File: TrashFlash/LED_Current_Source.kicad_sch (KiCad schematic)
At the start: 32 parts, among them IC2 ADG5419BCPZ-RL7, IC4 SN74LXC2T45QDTTRQ1, IC8 AD8615AUJZ-REEL, Q1 BC56-10PA,115, Q2 BC56-10PA,115, Q3 BC56-10PA,115, Q4 BC56-10PA,115, U1 SI5448DU-T1-GE3, U2 SI5448DU-T1-GE3

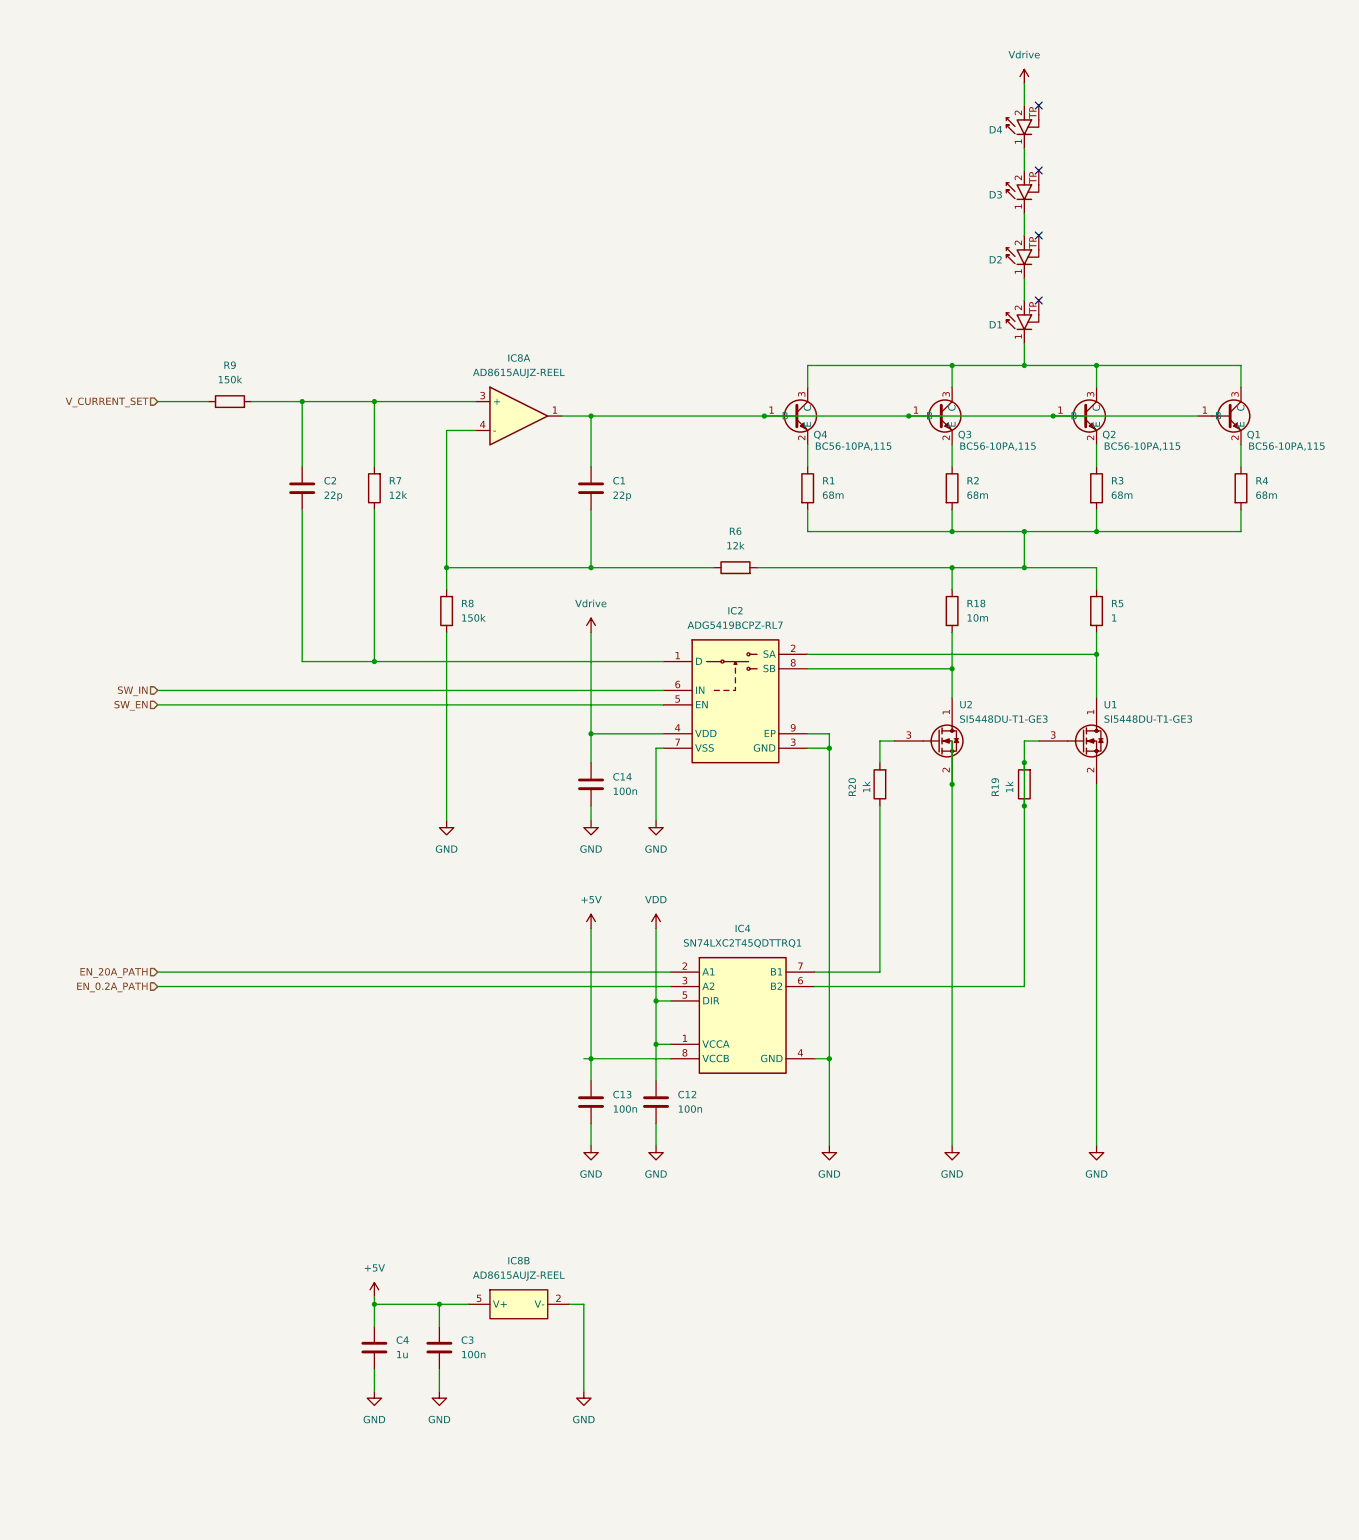
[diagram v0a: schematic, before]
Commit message: Added netlabels / cleaned up schematic
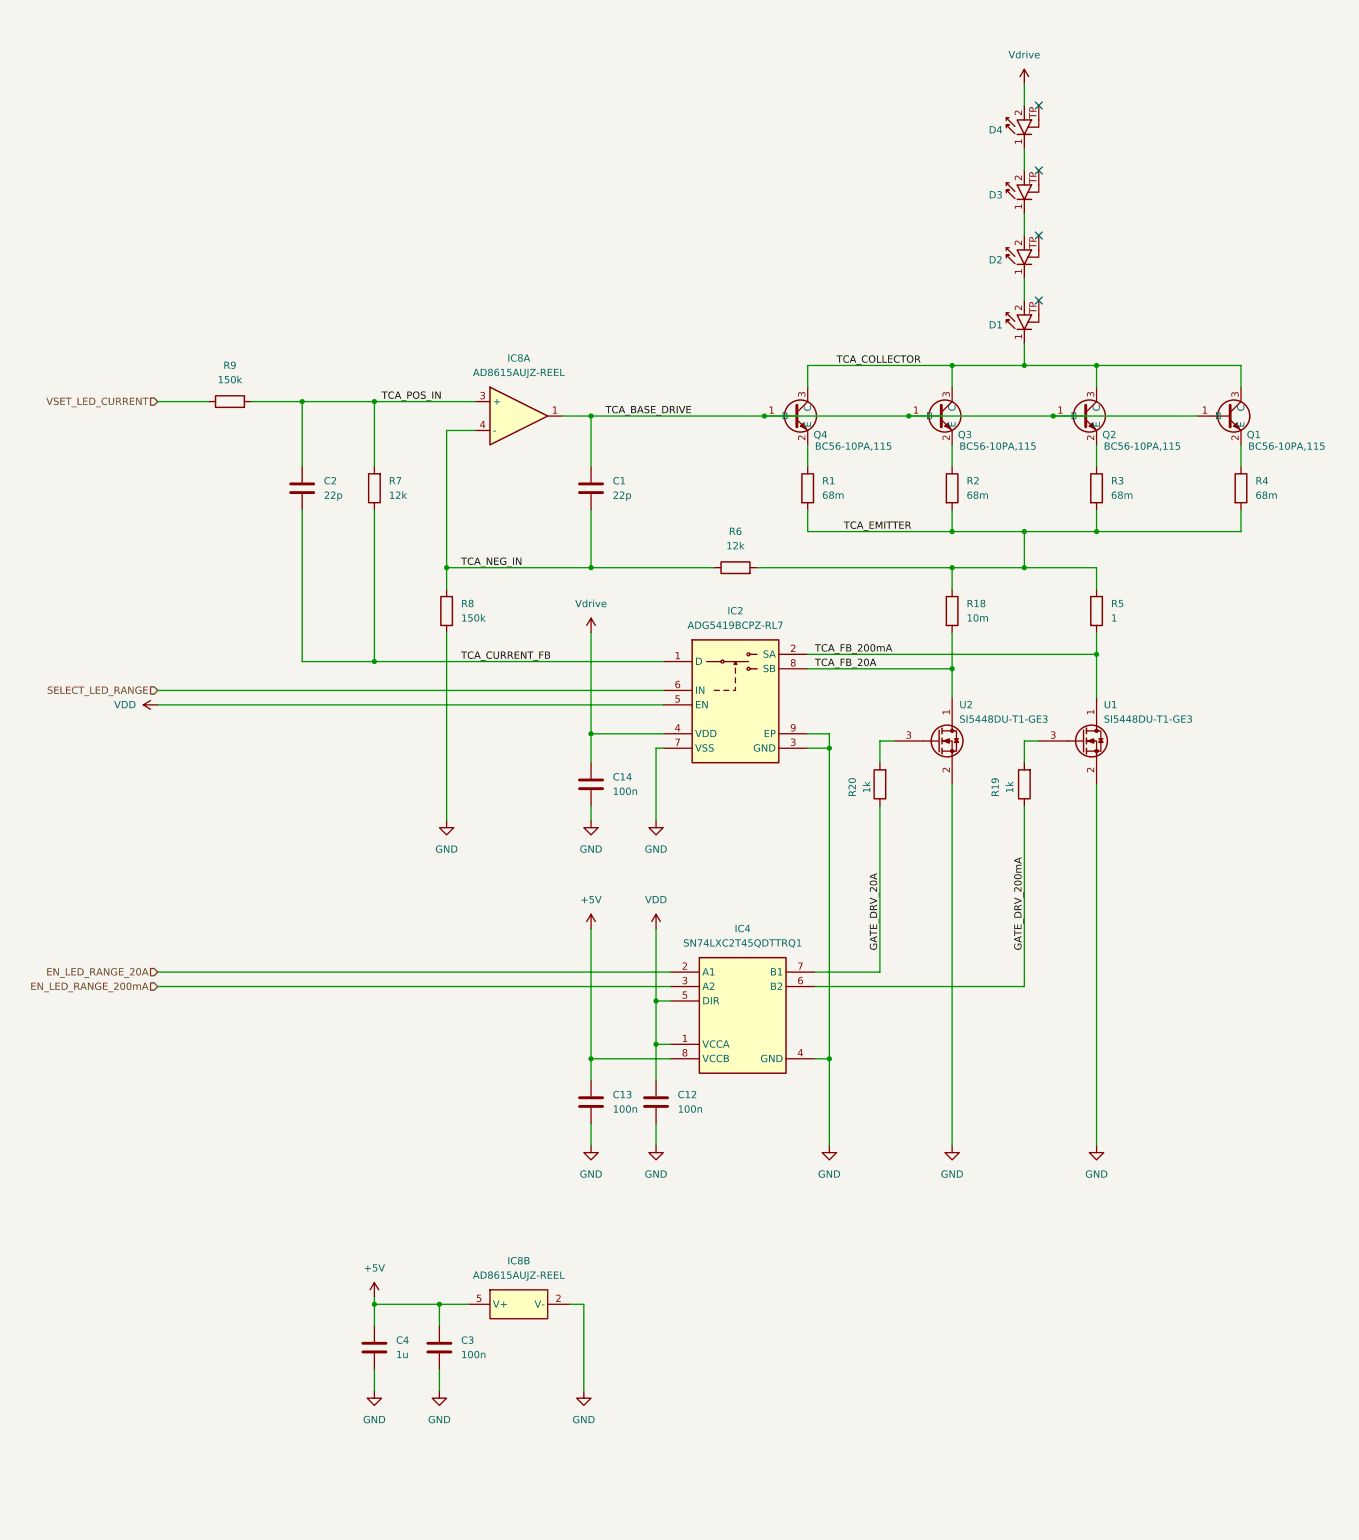
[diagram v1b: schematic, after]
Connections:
- net SW_EN is gone; now on net VDD: IC2.5 (EN)
- net TCA_FB_20A: now reaches IC2.8 (SB), R18.2, U2.1
- net TCA_EMITTER: now reaches R1.2, R18.1, R2.2, R3.2, R4.2, R5.1, R6.2
- net TCA_NEG_IN: now reaches C1.2, IC8.4 (-), R6.1, R8.2
- net TCA_CURRENT_FB: now reaches C2.1, IC2.1 (D), R7.1
- net TCA_FB_200mA: now reaches IC2.2 (SA), R5.2, U1.1
- net TCA_BASE_DRIVE: now reaches C1.1, IC8.1, Q1.1 (B), Q2.1 (B), Q3.1 (B), Q4.1 (B)
- net TCA_COLLECTOR: now reaches D1.1 (K), Q1.3 (C), Q2.3 (C), Q3.3 (C), Q4.3 (C)
- net at R19.2, U1.3: no longer IC4.6 (B2), R19.1
- net TCA_POS_IN: now reaches C2.2, IC8.3 (+), R7.2, R9.2
- net GATE_DRV_20A: now reaches IC4.7 (B1), R20.1
- net EN_0.2A_PATH renamed EN_LED_RANGE_200mA
- net EN_20A_PATH renamed EN_LED_RANGE_20A
- net SW_IN renamed SELECT_LED_RANGE
- net V_CURRENT_SET renamed VSET_LED_CURRENT
- new net GATE_DRV_200mA: IC4.6 (B2), R19.1
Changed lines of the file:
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@@
 	)
 	(junction
-		(at 276.86 144.78)
-		(diameter 0)
-		(color 0 0 0 0)
-	)
-	(junction
 		(at 276.86 110.49)
 		(diameter 0)
@@
 	)
 	(junction
-		(at 276.86 152.4)
-		(diameter 0)
-		(color 0 0 0 0)
-	)
-	(junction
 		(at 149.86 81.28)
 		(diameter 0)
 		(color 0 0 0 0)
 	)
-	(junction
-		(at 264.16 148.59)
-		(diameter 0)
-		(color 0 0 0 0)
-	)
 	(no_connect
 		(at 279.4 52.07)
@@
 	(wire
 		(pts
-			(xy 276.86 144.78) (xy 276.86 152.4)
-		)
-		(stroke
-			(width 0)
-			(type default)
-		)
-	)
-	(wire
-		(pts
 			(xy 173.99 240.03) (xy 179.07 240.03)
 		)
@@
 	(wire
 		(pts
-			(xy 264.16 140.97) (xy 264.16 148.59)
-		)
-		(stroke
-			(width 0)
-			(type default)
-		)
-	)
-	(wire
-		(pts
 			(xy 242.57 196.85) (xy 242.57 212.09)
 		)
@@
 	(wire
 		(pts
-			(xy 276.86 152.4) (xy 276.86 184.15)
-		)
-		(stroke
-			(width 0)
-			(type default)
-		)
-	)
-	(wire
-		(pts
 			(xy 200.66 83.82) (xy 231.14 83.82)
 		)
@@
 	(wire
 		(pts
-			(xy 251.46 152.4) (xy 251.46 181.61)
+			(xy 276.86 152.4) (xy 276.86 184.15)
 		)
 		(stroke
@@
 	(wire
 		(pts
-			(xy 200.66 196.85) (xy 199.39 196.85)
-		)
-		(stroke
-			(width 0)
-			(type default)
-		)
-	)
-	(wire
-		(pts
 			(xy 264.16 128.27) (xy 264.16 133.35)
 		)
@@
 	(wire
 		(pts
+			(xy 251.46 152.4) (xy 251.46 181.61)
+		)
+		(stroke
+			(width 0)
+			(type default)
+		)
+	)
+	(wire
+		(pts
 			(xy 242.57 139.7) (xy 242.57 142.24)
 		)
@@
 		)
 	)
-	(hierarchical_label "EN_20A_PATH"
-		(shape input)
-		(at 124.46 181.61 180)
+	(label "GATE_DRV_200mA"
+		(at 276.86 177.8 90)
 		(effects
 			(font
 				(size 1.27 1.27)
 			)
-			(justify right)
+			(justify left bottom)
+		)
+	)
+	(label "TCA_POS_IN"
+		(at 163.83 81.28 0)
+		(effects
+			(font
+				(size 1.27 1.27)
+			)
+			(justify left bottom)
+		)
+	)
+	(label "TCA_COLLECTOR"
+		(at 243.84 74.93 0)
+		(effects
+			(font
+				(size 1.27 1.27)
+			)
+			(justify left bottom)
+		)
+	)
+	(label "TCA_BASE_DRIVE"
+		(at 203.2 83.82 0)
+		(effects
+			(font
+				(size 1.27 1.27)
+			)
+			(justify left bottom)
 		)
 	)
-	(hierarchical_label "V_CURRENT_SET"
+	(label "GATE_DRV_20A"
+		(at 251.46 177.8 90)
+		(effects
+			(font
+				(size 1.27 1.27)
+			)
+			(justify left bottom)
+		)
+	)
+	(label "TCA_CURRENT_FB"
+		(at 177.8 127 0)
+		(effects
+			(font
+				(size 1.27 1.27)
+			)
+			(justify left bottom)
+		)
+	)
+	(label "TCA_EMITTER"
+		(at 245.11 104.14 0)
+		(effects
+			(font
+				(size 1.27 1.27)
+			)
+			(justify left bottom)
+		)
+	)
+	(label "TCA_NEG_IN"
+		(at 177.8 110.49 0)
+		(effects
+			(font
+				(size 1.27 1.27)
+			)
+			(justify left bottom)
+		)
+	)
+	(label "TCA_FB_20A"
+		(at 240.03 128.27 0)
+		(effects
+			(font
+				(size 1.27 1.27)
+			)
+			(justify left bottom)
+		)
+	)
+	(label "TCA_FB_200mA"
+		(at 240.03 125.73 0)
+		(effects
+			(font
+				(size 1.27 1.27)
+			)
+			(justify left bottom)
+		)
+	)
+	(hierarchical_label "EN_LED_RANGE_20A"
 		(shape input)
-		(at 124.46 81.28 180)
+		(at 124.46 181.61 180)
 		(effects
 			(font
@@
 		)
 	)
-	(hierarchical_label "SW_IN"
+	(hierarchical_label "VSET_LED_CURRENT"
 		(shape input)
-		(at 124.46 132.08 180)
+		(at 124.46 81.28 180)
 		(effects
 			(font
@@
 		)
 	)
-	(hierarchical_label "SW_EN"
+	(hierarchical_label "SELECT_LED_RANGE"
 		(shape input)
-		(at 124.46 134.62 180)
+		(at 124.46 132.08 180)
 		(effects
 			(font
@@
 		)
 	)
-	(hierarchical_label "EN_0.2A_PATH"
+	(hierarchical_label "EN_LED_RANGE_200mA"
 		(shape input)
 		(at 124.46 184.15 180)
@@
 					(unit 1)
 				)
+			)
+		)
+	)
+	(symbol
+		(lib_id "power:VDD")
+		(at 124.46 134.62 90)
+		(unit 1)
+		(exclude_from_sim no)
+		(in_bom yes)
+		(on_board yes)
+		(dnp no)
+		(fields_autoplaced yes)
+		(property "Reference" "#PWR061"
+			(at 128.27 134.62 0)
+			(effects
+				(font
+					(size 1.27 1.27)
+				)
+				(hide yes)
+			)
+		)
+		(property "Value" "VDD"
+			(at 120.65 134.6199 90)
+			(effects
+				(font
+					(size 1.27 1.27)
+				)
+				(justify left)
+			)
+		)
+		(property "Footprint" ""
+			(at 124.46 134.62 0)
+			(effects
+				(font
+					(size 1.27 1.27)
+				)
+				(hide yes)
+			)
+		)
+		(property "Datasheet" ""
+			(at 124.46 134.62 0)
+			(effects
+				(font
+					(size 1.27 1.27)
+				)
+				(hide yes)
+			)
+		)
+		(property "Description" "Power symbol creates a global label with name \"VDD\""
+			(at 124.46 134.62 0)
+			(effects
+				(font
+					(size 1.27 1.27)
+				)
+				(hide yes)
+			)
+		)
+		(pin "1"
+		)
+		(instances
+			(project "TrashFlash"
+				(path "/256082dc-9c82-41ae-bfb7-0b4bd4121c78/b540a372-b28b-49dd-801f-e36c7fece9b9"
+					(reference "#PWR061")
+					(unit 1)
+				)

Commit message: Added 3D-models to footprints, PCB outline and component placement
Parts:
- IC2: footprint SON50P300X200X80-9N-D -> TrashFlash:SON50P300X200X80-9N-D
- IC4: footprint SN74LXC2T45QDTTRQ1 -> TrashFlash:SN74LXC2T45QDTTRQ1
- IC8: footprint SOT95P280X100-5N -> TrashFlash:SOT95P280X100-5N
- Q1, Q2, Q3, Q4: footprint PTVS24VZ1UPAZ -> TrashFlash:PTVS24VZ1UPAZ
- U1, U2: footprint SI5448DUT1GE3 -> TrashFlash:SI5448DUT1GE3
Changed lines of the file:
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@@
 			)
 		)
-		(property "Footprint" "SI5448DUT1GE3"
+		(property "Footprint" "TrashFlash:SI5448DUT1GE3"
 			(at 285.75 235.89 0)
 			(effects
@@
 			)
 		)
-		(property "Footprint" "SON50P300X200X80-9N-D"
+		(property "Footprint" "TrashFlash:SON50P300X200X80-9N-D"
 			(at 226.314 145.796 0)
 			(effects
@@
 			)
 		)
-		(property "Footprint" "SOT95P280X100-5N"
+		(property "Footprint" "TrashFlash:SOT95P280X100-5N"
 			(at 209.55 334.95 0)
 			(effects
@@
 			)
 		)
-		(property "Footprint" "PTVS24VZ1UPAZ"
+		(property "Footprint" "TrashFlash:PTVS24VZ1UPAZ"
 			(at 262.636 96.774 0)
 			(effects
@@
 			)
 		)
-		(property "Footprint" "PTVS24VZ1UPAZ"
+		(property "Footprint" "TrashFlash:PTVS24VZ1UPAZ"
 			(at 313.436 96.774 0)
 			(effects
@@
 			)
 		)
-		(property "Footprint" "SOT95P280X100-5N"
+		(property "Footprint" "TrashFlash:SOT95P280X100-5N"
 			(at 207.01 178.74 0)
 			(effects
@@
 			)
 		)
-		(property "Footprint" "SN74LXC2T45QDTTRQ1"
+		(property "Footprint" "TrashFlash:SN74LXC2T45QDTTRQ1"
 			(at 251.46 273.99 0)
 			(effects
@@
 			)
 		)
-		(property "Footprint" "PTVS24VZ1UPAZ"
+		(property "Footprint" "TrashFlash:PTVS24VZ1UPAZ"
 			(at 237.236 96.774 0)
 			(effects
@@
 			)
 		)
-		(property "Footprint" "PTVS24VZ1UPAZ"
+		(property "Footprint" "TrashFlash:PTVS24VZ1UPAZ"
 			(at 288.036 96.774 0)
 			(effects
@@
 			)
 		)
-		(property "Footprint" "SI5448DUT1GE3"
+		(property "Footprint" "TrashFlash:SI5448DUT1GE3"
 			(at 311.15 235.89 0)
 			(effects
